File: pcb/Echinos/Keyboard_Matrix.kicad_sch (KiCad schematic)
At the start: 61 parts, among them J5 Joystick

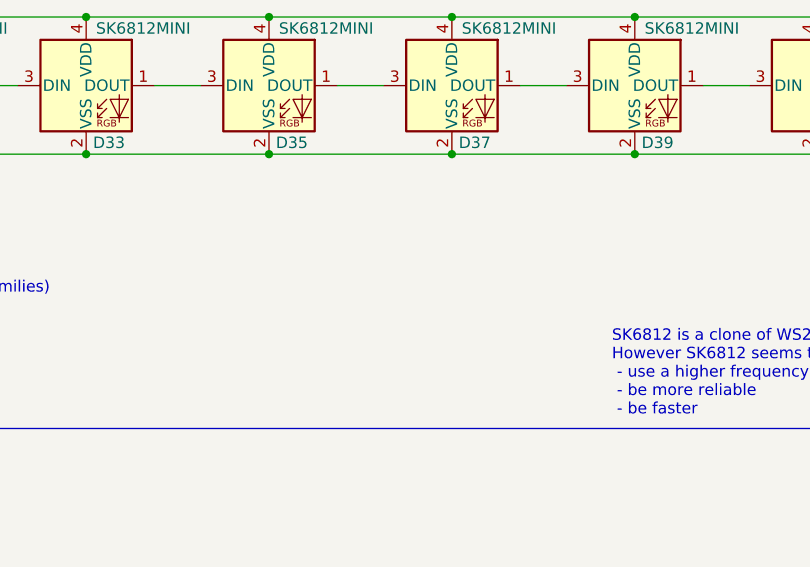
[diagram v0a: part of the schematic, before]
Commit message: ♻️ [PCB] - Fill / Check LCSC part number. Still some parts without a number:   - FPC connectors   - SATA connector   - Reset / Bootloader switches   - LED
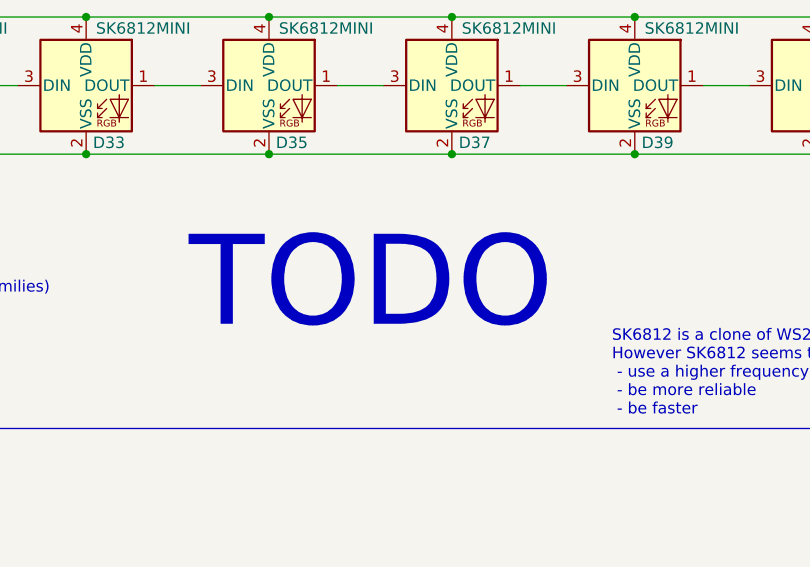
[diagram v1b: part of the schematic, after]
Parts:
- J5, S1, S10, S11, S12, S13, S14, S15, S16, S17, S18, S19, S3, S5, S6, S8, S9: now left out of the parts list
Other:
- note added: "TODO"
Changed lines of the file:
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@@
     (effects (font (size 1.27 1.27)) (justify left bottom))
+  )
+  (text "TODO" (at 154.94 -19.05 0)
+    (effects (font (size 10 10)) (justify left bottom))
   )
   (text "Rotary encoder / Switch" (at 25.4 24.13 0)
@@
   )
   (symbol (lib_id "Switch:SW_Push") (at 35.56 135.89 0) (unit 1)
-    (in_bom yes) (on_board yes) (dnp no)
+    (in_bom no) (on_board yes) (dnp no)
     (property "Reference" "S3" (at 39.37 133.096 0)
       (effects (font (size 1.27 1.27)))
@@
   )
   (symbol (lib_id "Switch:SW_Push") (at 53.34 151.13 0) (unit 1)
-    (in_bom yes) (on_board yes) (dnp no)
+    (in_bom no) (on_board yes) (dnp no)
     (property "Reference" "S8" (at 57.15 148.59 0)
       (effects (font (size 1.27 1.27)))
@@
   )
   (symbol (lib_id "Switch:SW_Push") (at 71.12 135.89 0) (unit 1)
-    (in_bom yes) (on_board yes) (dnp no)
+    (in_bom no) (on_board yes) (dnp no)
     (property "Reference" "S11" (at 74.93 133.096 0)
       (effects (font (size 1.27 1.27)))
@@
   )
   (symbol (lib_id "Switch:SW_Push") (at 88.9 105.41 0) (unit 1)
-    (in_bom yes) (on_board yes) (dnp no)
+    (in_bom no) (on_board yes) (dnp no)
     (property "Reference" "S13" (at 92.71 102.616 0)
       (effects (font (size 1.27 1.27)))
@@
   )
   (symbol (lib_id "Switch:SW_Push") (at 106.68 135.89 0) (unit 1)
-    (in_bom yes) (on_board yes) (dnp no)
+    (in_bom no) (on_board yes) (dnp no)
     (property "Reference" "S19" (at 110.49 133.096 0)
       (effects (font (size 1.27 1.27)))
@@
   )
   (symbol (lib_id "Switch:SW_Push") (at 53.34 120.65 0) (unit 1)
-    (in_bom yes) (on_board yes) (dnp no)
+    (in_bom no) (on_board yes) (dnp no)
     (property "Reference" "S6" (at 57.15 117.856 0)
       (effects (font (size 1.27 1.27)))
@@
   )
   (symbol (lib_id "Switch:SW_Push") (at 71.12 105.41 0) (unit 1)
-    (in_bom yes) (on_board yes) (dnp no)
+    (in_bom no) (on_board yes) (dnp no)
     (property "Reference" "S9" (at 74.93 102.616 0)
       (effects (font (size 1.27 1.27)))
@@
   )
   (symbol (lib_id "Switch:SW_Push") (at 53.34 105.41 0) (unit 1)
-    (in_bom yes) (on_board yes) (dnp no)
+    (in_bom no) (on_board yes) (dnp no)
     (property "Reference" "S5" (at 57.15 102.616 0)
       (effects (font (size 1.27 1.27)))
@@
   )
   (symbol (lib_id "Switch:SW_Push") (at 88.9 120.65 0) (unit 1)
-    (in_bom yes) (on_board yes) (dnp no)
+    (in_bom no) (on_board yes) (dnp no)
     (property "Reference" "S14" (at 92.71 117.856 0)
       (effects (font (size 1.27 1.27)))
@@
   )
   (symbol (lib_id "Switch:SW_Push") (at 106.68 105.41 0) (unit 1)
-    (in_bom yes) (on_board yes) (dnp no)
+    (in_bom no) (on_board yes) (dnp no)
     (property "Reference" "S17" (at 110.49 102.616 0)
       (effects (font (size 1.27 1.27)))
@@
   )
   (symbol (lib_id "Switch:SW_Push") (at 106.68 151.13 0) (unit 1)
-    (in_bom yes) (on_board yes) (dnp no)
+    (in_bom no) (on_board yes) (dnp no)
     (property "Reference" "S16" (at 110.49 148.336 0)
       (effects (font (size 1.27 1.27)))
@@
   )
   (symbol (lib_id "Connector:Conn_01x06_Socket") (at 105.41 40.64 0) (unit 1)
-    (in_bom yes) (on_board yes) (dnp no)
+    (in_bom no) (on_board yes) (dnp no)
     (property "Reference" "J5" (at 100.33 29.21 0)
       (effects (font (size 1.27 1.27)) (justify left))
@@
   )
   (symbol (lib_id "Switch:SW_Push") (at 71.12 120.65 0) (unit 1)
-    (in_bom yes) (on_board yes) (dnp no)
+    (in_bom no) (on_board yes) (dnp no)
     (property "Reference" "S10" (at 74.93 117.856 0)
       (effects (font (size 1.27 1.27)))
@@
   )
   (symbol (lib_id "Switch:SW_Push") (at 106.68 120.65 0) (unit 1)
-    (in_bom yes) (on_board yes) (dnp no)
+    (in_bom no) (on_board yes) (dnp no)
     (property "Reference" "S18" (at 110.49 117.856 0)
       (effects (font (size 1.27 1.27)))
@@
   )
   (symbol (lib_id "Switch:SW_Push") (at 71.12 151.13 0) (unit 1)
-    (in_bom yes) (on_board yes) (dnp no)
+    (in_bom no) (on_board yes) (dnp no)
     (property "Reference" "S12" (at 74.93 148.336 0)
       (effects (font (size 1.27 1.27)))
@@
   )
   (symbol (lib_id "Switch:SW_Push") (at 88.9 151.13 0) (unit 1)
-    (in_bom yes) (on_board yes) (dnp no)
+    (in_bom no) (on_board yes) (dnp no)
     (property "Reference" "S16" (at 92.71 148.336 0)
       (effects (font (size 1.27 1.27)))
@@
   )
   (symbol (lib_id "Switch:SW_Push") (at 88.9 135.89 0) (unit 1)
-    (in_bom yes) (on_board yes) (dnp no)
+    (in_bom no) (on_board yes) (dnp no)
     (property "Reference" "S15" (at 92.71 133.096 0)
       (effects (font (size 1.27 1.27)))
@@
   )
   (symbol (lib_id "Device:RotaryEncoder_Switch") (at 43.18 45.72 90) (mirror x) (unit 1)
-    (in_bom yes) (on_board yes) (dnp no)
+    (in_bom no) (on_board yes) (dnp no)
     (property "Reference" "S1" (at 50.8 45.72 90)
       (effects (font (size 1.27 1.27)) (justify right))

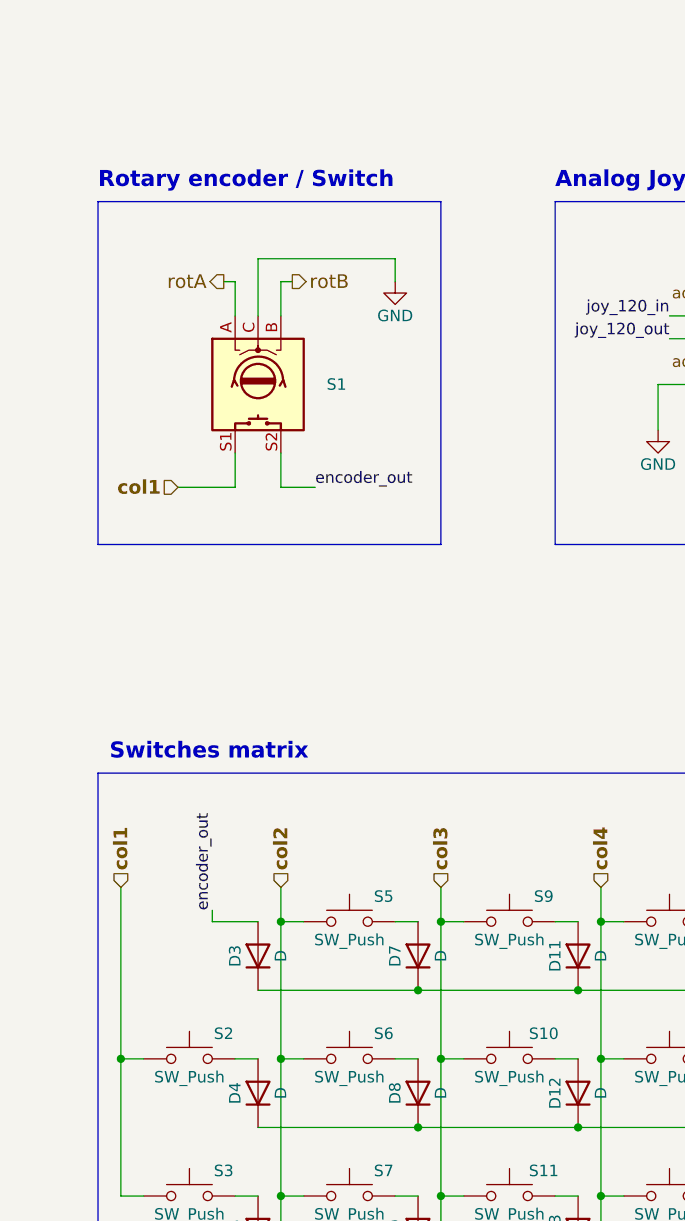
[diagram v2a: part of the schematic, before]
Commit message: 💥 [PCB] - Remove encoder on top pinky as this key is now used in my current layout thanks to alt fingering removing the awkward movement required to move the pinky up. Not sure i will put and encoder somewhere as I find little to no use for them.
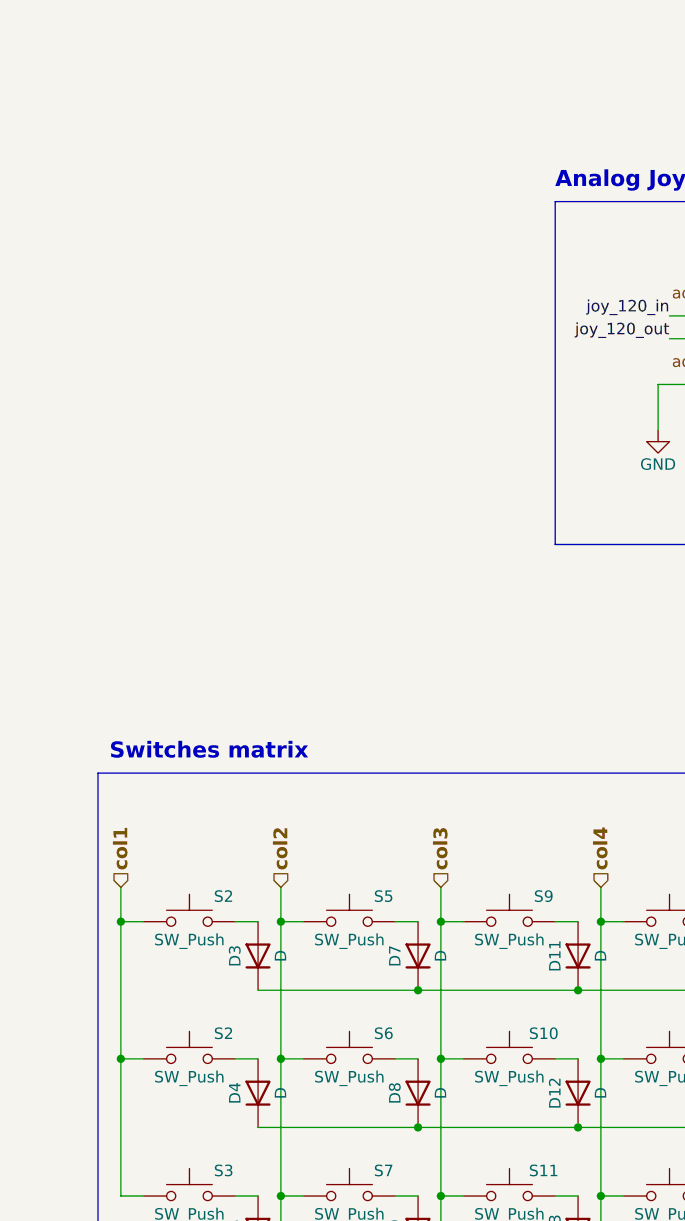
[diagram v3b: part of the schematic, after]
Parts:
- removed S1: RotaryEncoder_Switch, Echinos:SW_Choc_MX_KS33_1u_hotswap_EC12E, symbol Device:RotaryEncoder_Switch
- added S2: SW_Push, Echinos:SW_Choc_MX_KS33_1u_hotswap, symbol Switch:SW_Push
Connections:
- net col1: now also S2.1
- net encoder_out: no longer names the net of D3.2 (A)
- net encoder_out: now also S2.2
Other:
- note removed: "Rotary encoder / Switch"
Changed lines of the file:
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@@
   (junction (at 123.19 -85.09) (diameter 0) (color 0 0 0 0)
+  )
+  (junction (at 27.94 105.41) (diameter 0) (color 0 0 0 0)
   )
   (junction (at 27.94 120.65) (diameter 0) (color 0 0 0 0)
@@
     (stroke (width 0) (type default))
   )
-  (wire (pts (xy 43.18 31.75) (xy 43.18 38.1))
-    (stroke (width 0) (type default))
-  )
-  (wire (pts (xy 58.42 31.75) (xy 43.18 31.75))
-    (stroke (width 0) (type default))
-  )
   (wire (pts (xy 102.87 -54.61) (xy 123.19 -54.61))
     (stroke (width 0) (type default))
@@
     (stroke (width 0) (type default))
   )
+  (wire (pts (xy 27.94 105.41) (xy 27.94 120.65))
+    (stroke (width 0) (type default))
+  )
   (wire (pts (xy 95.25 55.88) (xy 100.33 55.88))
     (stroke (width 0) (type default))
@@
     (stroke (width 0) (type default))
   )
-  (wire (pts (xy 43.18 105.41) (xy 38.1 105.41))
-    (stroke (width 0) (type default))
-  )
   (wire (pts (xy 99.06 151.13) (xy 101.6 151.13))
     (stroke (width 0) (type default))
@@
     (stroke (width 0) (type default))
   )
+  (wire (pts (xy 40.64 105.41) (xy 43.18 105.41))
+    (stroke (width 0) (type default))
+  )
   (wire (pts (xy 43.18 143.51) (xy 60.96 143.51))
     (stroke (width 0) (type default))
@@
     (stroke (width 0) (type default))
   )
-  (wire (pts (xy 45.72 34.29) (xy 46.99 34.29))
-    (stroke (width 0) (type default))
-  )
   (wire (pts (xy 76.2 120.65) (xy 78.74 120.65))
     (stroke (width 0) (type default))
@@
     (stroke (width 0) (type default))
   )
-  (wire (pts (xy 45.72 34.29) (xy 45.72 38.1))
-    (stroke (width 0) (type default))
-  )
   (wire (pts (xy 163.83 -54.61) (xy 184.15 -54.61))
     (stroke (width 0) (type default))
@@
     (stroke (width 0) (type default))
   )
+  (wire (pts (xy 27.94 105.41) (xy 30.48 105.41))
+    (stroke (width 0) (type default))
+  )
   (wire (pts (xy 191.77 -46.99) (xy 196.85 -46.99))
     (stroke (width 0) (type default))
@@
     (stroke (width 0) (type default))
   )
-  (wire (pts (xy 34.29 57.15) (xy 40.64 57.15))
-    (stroke (width 0) (type default))
-  )
   (wire (pts (xy 60.96 165.1) (xy 78.74 165.1))
     (stroke (width 0) (type default))
@@
     (stroke (width 0) (type default))
   )
-  (wire (pts (xy 49.53 57.15) (xy 45.72 57.15))
-    (stroke (width 0) (type default))
-  )
   (wire (pts (xy 184.15 -39.37) (xy 204.47 -39.37))
     (stroke (width 0) (type default))
@@
     (stroke (width 0) (type default))
   )
-  (wire (pts (xy 27.94 101.6) (xy 27.94 120.65))
+  (wire (pts (xy 27.94 101.6) (xy 27.94 105.41))
     (stroke (width 0) (type default))
   )
@@
     (stroke (width 0) (type default))
   )
-  (wire (pts (xy 40.64 34.29) (xy 40.64 38.1))
-    (stroke (width 0) (type default))
-  )
   (wire (pts (xy 224.79 -39.37) (xy 245.11 -39.37))
     (stroke (width 0) (type default))
@@
     (stroke (width 0) (type default))
   )
-  (wire (pts (xy 40.64 53.34) (xy 40.64 57.15))
-    (stroke (width 0) (type default))
-  )
   (wire (pts (xy 99.06 120.65) (xy 101.6 120.65))
     (stroke (width 0) (type default))
@@
     (stroke (width 0) (type default))
   )
-  (wire (pts (xy 38.1 105.41) (xy 38.1 104.14))
-    (stroke (width 0) (type default))
-  )
   (wire (pts (xy 81.28 101.6) (xy 81.28 105.41))
     (stroke (width 0) (type default))
@@
     (stroke (width 0) (type default))
   )
-  (wire (pts (xy 40.64 34.29) (xy 39.37 34.29))
-    (stroke (width 0) (type default))
-  )
   (wire (pts (xy 90.17 -46.99) (xy 95.25 -46.99))
     (stroke (width 0) (type default))
@@
     (stroke (width 0) (type default))
   )
-  (wire (pts (xy 45.72 57.15) (xy 45.72 53.34))
-    (stroke (width 0) (type default))
-  )
   (wire (pts (xy 81.28 120.65) (xy 81.28 135.89))
     (stroke (width 0) (type default))
@@
     (stroke (width 0) (type default))
   )
-  (wire (pts (xy 58.42 34.29) (xy 58.42 31.75))
-    (stroke (width 0) (type default))
-  )
   (wire (pts (xy 58.42 135.89) (xy 60.96 135.89))
     (stroke (width 0) (type default))
@@
   )
   (rectangle (start 16.51 -92.71) (end 270.51 -8.89)
-    (stroke (width 0) (type default))
-    (fill (type none))
-  )
-  (rectangle (start 25.4 25.4) (end 63.5 63.5)
     (stroke (width 0) (type default))
     (fill (type none))
@@
     (effects (font (size 10 10)) (justify left bottom))
   )
-  (text "Rotary encoder / Switch" (at 25.4 24.13 0)
-    (effects (font (size 1.778 1.778) (thickness 0.3556) bold) (justify left bottom))
-  )
   (text "ROWS 3-4" (at 43.18 -54.61 0)
     (effects (font (size 1.27 1.27) (thickness 0.254) bold) (justify left bottom))
@@
     (effects (font (size 1.27 1.27)) (justify left bottom))
   )
-  (label "encoder_out" (at 38.1 104.14 90) (fields_autoplaced)
-    (effects (font (size 1.27 1.27)) (justify left bottom))
-  )
   (label "joy_120_out" (at 88.9 40.64 180) (fields_autoplaced)
     (effects (font (size 1.27 1.27)) (justify right bottom))
   )
-  (label "encoder_out" (at 49.53 57.15 0) (fields_autoplaced)
-    (effects (font (size 1.27 1.27)) (justify left bottom))
-  )
   (label "joy_120_out" (at 111.76 153.67 270) (fields_autoplaced)
     (effects (font (size 1.27 1.27)) (justify right bottom))
@@
     (effects (font (size 1.27 1.27)) (justify right))
   )
-  (hierarchical_label "rotB" (shape output) (at 46.99 34.29 0) (fields_autoplaced)
-    (effects (font (size 1.524 1.524)) (justify left))
-  )
   (hierarchical_label "col4" (shape input) (at 81.28 101.6 90) (fields_autoplaced)
     (effects (font (size 1.524 1.524) (thickness 0.3048) bold) (justify left))
@@
     (effects (font (size 1.524 1.524) (thickness 0.3048) bold) (justify left))
   )
-  (hierarchical_label "rotA" (shape output) (at 39.37 34.29 180) (fields_autoplaced)
-    (effects (font (size 1.524 1.524)) (justify right))
-  )
   (hierarchical_label "row4" (shape output) (at 123.19 165.1 0) (fields_autoplaced)
     (effects (font (size 1.524 1.524) (thickness 0.3048) bold) (justify left))
@@
     (effects (font (size 1.524 1.524) (thickness 0.3048) bold) (justify left))
   )
-  (hierarchical_label "col1" (shape input) (at 34.29 57.15 180) (fields_autoplaced)
-    (effects (font (size 1.524 1.524) (thickness 0.3048) bold) (justify right))
-  )
   (symbol (lib_id "Device:D") (at 60.96 154.94 90) (unit 1)
     (in_bom yes) (on_board yes) (dnp no)
@@
         (path "/5bd3006d-ec09-4ffb-bec3-03fa5613b46a/82089e05-aeac-4bc0-b466-29ce28ef1ab1/68cfefc1-3239-4b03-a7c8-c56ddb495d3c"
           (reference "D34") (unit 1)
-        )
-      )
-    )
-  )
-  (symbol (lib_id "power:GND") (at 58.42 34.29 0) (unit 1)
-    (in_bom yes) (on_board yes) (dnp no)
-    (property "Reference" "#PWR036" (at 58.42 40.64 0)
-      (effects (font (size 1.27 1.27)) hide)
-    )
-    (property "Value" "GND" (at 58.42 38.1 0)
-      (effects (font (size 1.27 1.27)))
-    )
-    (property "Footprint" "" (at 58.42 34.29 0)
-      (effects (font (size 1.27 1.27)) hide)
-    )
-    (property "Datasheet" "" (at 58.42 34.29 0)
-      (effects (font (size 1.27 1.27)) hide)
-    )
-    (pin "1")
-    (instances
-      (project "Echinos"
-        (path "/5bd3006d-ec09-4ffb-bec3-03fa5613b46a/82089e05-aeac-4bc0-b466-29ce28ef1ab1"
-          (reference "#PWR036") (unit 1)
-        )
-        (path "/5bd3006d-ec09-4ffb-bec3-03fa5613b46a/82089e05-aeac-4bc0-b466-29ce28ef1ab1/68cfefc1-3239-4b03-a7c8-c56ddb495d3c"
-          (reference "#PWR039") (unit 1)
         )
       )
@@
         (path "/5bd3006d-ec09-4ffb-bec3-03fa5613b46a/82089e05-aeac-4bc0-b466-29ce28ef1ab1/68cfefc1-3239-4b03-a7c8-c56ddb495d3c"
           (reference "#PWR035") (unit 1)
+        )
+      )
+    )
+  )
+  (symbol (lib_id "Switch:SW_Push") (at 35.56 105.41 0) (unit 1)
+    (in_bom yes) (on_board yes) (dnp no)
+    (property "Reference" "S2" (at 39.37 102.616 0)
+      (effects (font (size 1.27 1.27)))
+    )
+    (property "Value" "SW_Push" (at 35.56 107.442 0)
+      (effects (font (size 1.27 1.27)))
+    )
+    (property "Footprint" "Echinos:SW_Choc_MX_KS33_1u_hotswap" (at 35.56 100.33 0)
+      (effects (font (size 1.27 1.27)) hide)
+    )
+    (property "Datasheet" "~" (at 35.56 100.33 0)
+      (effects (font (size 1.27 1.27)) hide)
+    )
+    (pin "1")
+    (pin "2")
+    (instances
+      (project "Echinos"
+        (path "/5bd3006d-ec09-4ffb-bec3-03fa5613b46a/82089e05-aeac-4bc0-b466-29ce28ef1ab1"
+          (reference "S2") (unit 1)
+        )
+        (path "/5bd3006d-ec09-4ffb-bec3-03fa5613b46a/82089e05-aeac-4bc0-b466-29ce28ef1ab1/68cfefc1-3239-4b03-a7c8-c56ddb495d3c"
+          (reference "SW101") (unit 1)
         )
       )
@@
         )
       )
-    )
-  )
-  (symbol (lib_id "Device:RotaryEncoder_Switch") (at 43.18 45.72 90) (mirror x) (unit 1)
-    (in_bom no) (on_board yes) (dnp no)
-    (property "Reference" "S1" (at 50.8 45.72 90)
-      (effects (font (size 1.27 1.27)) (justify right))
-    )
-    (property "Value" "RotaryEncoder_Switch" (at 49.53 44.4501 90)
-      (effects (font (size 1.27 1.27)) (justify right) hide)
-    )
-    (property "Footprint" "Echinos:SW_Choc_MX_KS33_1u_hotswap_EC12E" (at 39.116 41.91 0)
-      (effects (font (size 1.27 1.27)) hide)
-    )
-    (property "Datasheet" "~" (at 36.576 45.72 0)
-      (effects (font (size 1.27 1.27)) hide)
-    )
-    (pin "A")
-    (pin "B")
-    (pin "C")
-    (pin "S1" (alternate "1"))
-    (pin "S2" (alternate "2"))
-    (instances
-      (project "Echinos"
-        (path "/5bd3006d-ec09-4ffb-bec3-03fa5613b46a/82089e05-aeac-4bc0-b466-29ce28ef1ab1"
-          (reference "S1") (unit 1)
-        )
-        (path "/5bd3006d-ec09-4ffb-bec3-03fa5613b46a/82089e05-aeac-4bc0-b466-29ce28ef1ab1/68cfefc1-3239-4b03-a7c8-c56ddb495d3c"
-          (reference "SW101") (unit 1)
-        )
-      )
